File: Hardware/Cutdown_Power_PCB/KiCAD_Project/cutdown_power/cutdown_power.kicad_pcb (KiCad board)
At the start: 2 copper layers, 26.7 x 45.7 mm, 10 parts, among them J1 Control Signal, J2 Heater Coil, J3 Battery Pack, Q1 FQP30N06L

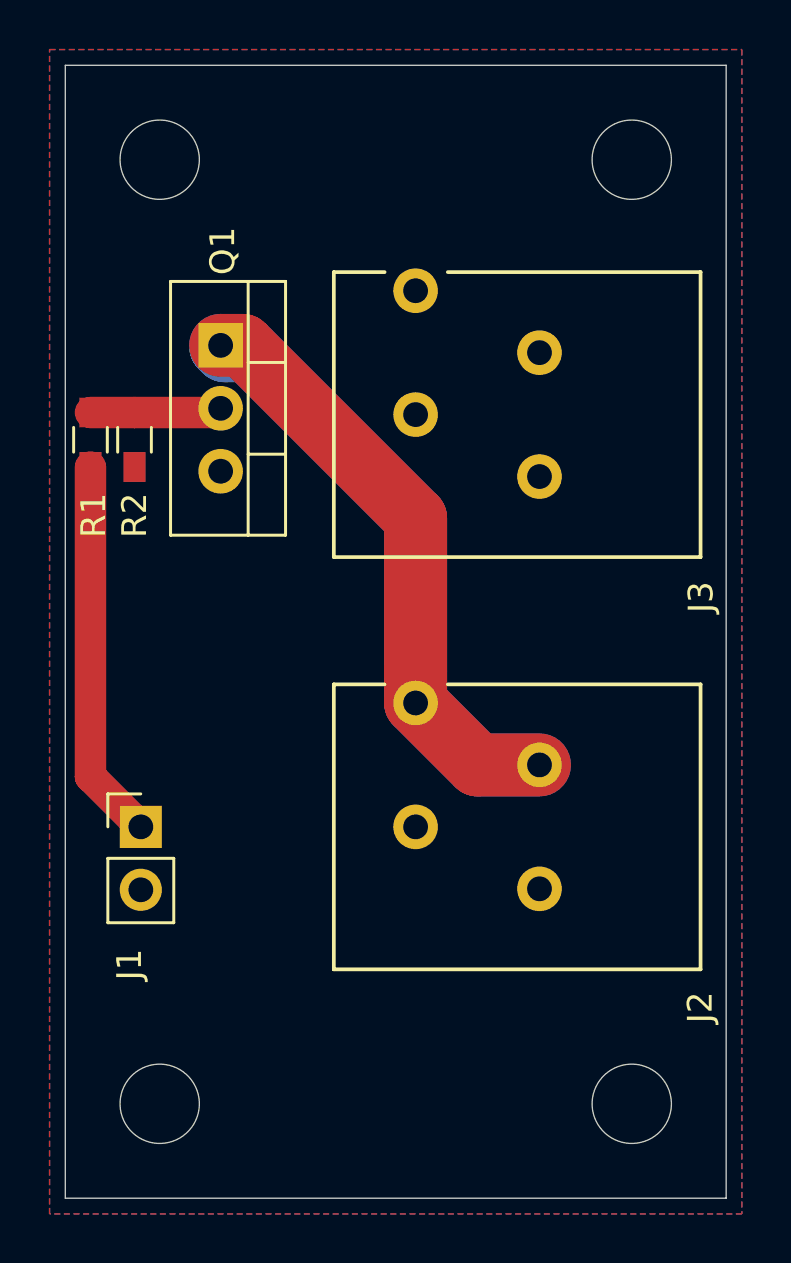
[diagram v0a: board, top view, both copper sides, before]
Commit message: Fix reversed Q1 issue and cut Rev 1.1
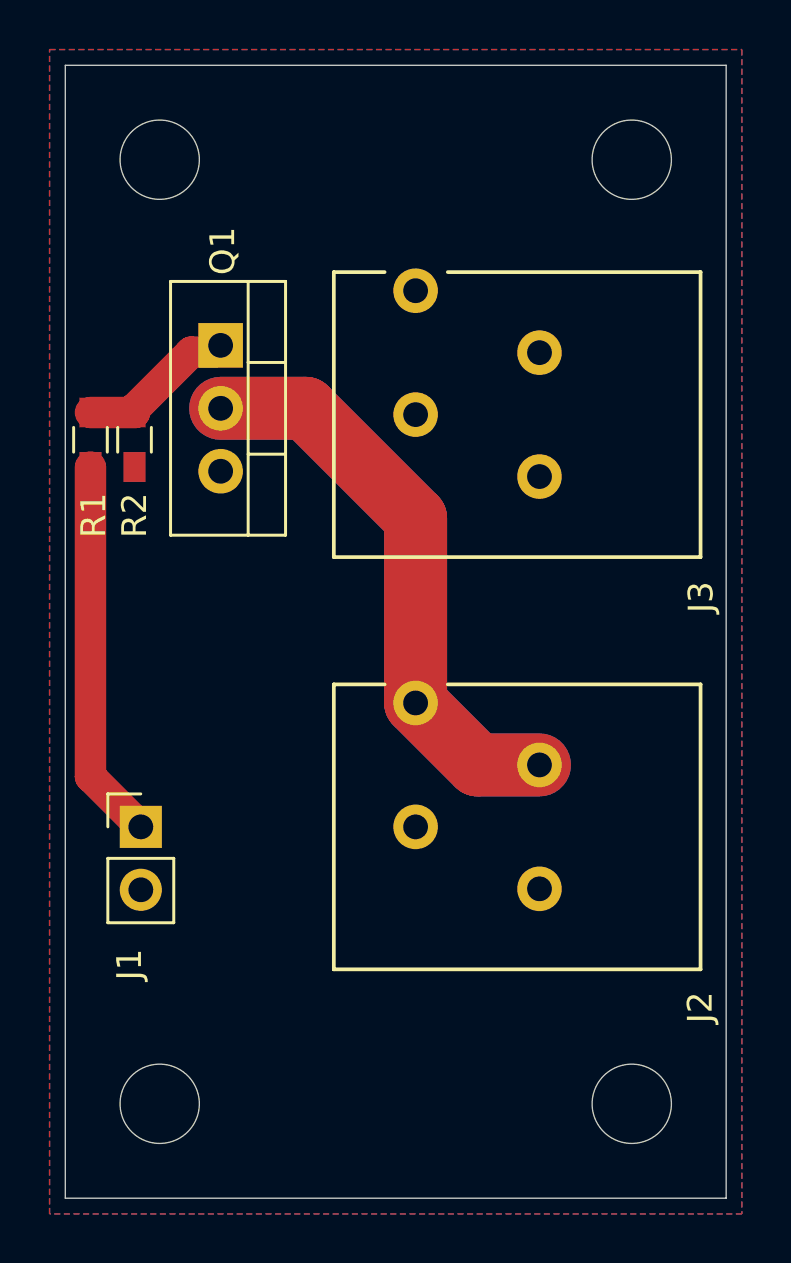
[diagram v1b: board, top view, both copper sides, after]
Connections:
- Q1 pad 1: Net-(J2-Pad2) -> Net-(Q1-Pad1)
- Q1 pad 2: Net-(Q1-Pad2) -> Net-(J2-Pad2)
- R1 pad 1: Net-(Q1-Pad2) -> Net-(Q1-Pad1)
- R2 pad 1: Net-(Q1-Pad2) -> Net-(Q1-Pad1)
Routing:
- net Net-(Q1-Pad1): track 0.00 -> 6.46 mm
- net Net-(Q1-Pad2): track 5.32 -> 0.00 mm
- net Net-(J2-Pad2): track 48.5 -> 46.4 mm
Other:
- board text added: "Leeman Geophysical LLC Cutdown Power Module Rev 1.1 December 2019 P/N 3-0000026"
- board text removed: "Leeman Geophysical LLC Cutdown Power Module Rev 1.0 November 2019 P/N 3-0000019"
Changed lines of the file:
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@@
     (thickness 1.6)
     (drawings 10)
-    (tracks 19)
+    (tracks 17)
     (zones 0)
     (modules 10)
@@
   (net 2 "Net-(J1-Pad1)")
   (net 3 "Net-(J2-Pad2)")
-  (net 4 "Net-(Q1-Pad2)")
-  (net 5 "Net-(J2-Pad1)")
+  (net 4 "Net-(J2-Pad1)")
+  (net 5 "Net-(Q1-Pad1)")
   (net_class Default "This is the default net class."
     (clearance 0.1524)
@@
     (add_net "Net-(J2-Pad1)")
     (add_net "Net-(J2-Pad2)")
-    (add_net "Net-(Q1-Pad2)")
+    (add_net "Net-(Q1-Pad1)")
   )
   (module Pin_Headers:Pin_Header_Straight_1x02_Pitch2.54mm (layer F.Cu)
@@
     (fp_line (start 5.75 -5.8) (end 5.75 -3.75) (layer F.SilkS) (width 0.15))
     (pad 1 thru_hole circle (at -2.5 2.5 90) (size 1.8 1.8) (drill 1) (layers *.Cu *.Mask)
-      (net 5 "Net-(J2-Pad1)"))
+      (net 4 "Net-(J2-Pad1)"))
     (pad 1 thru_hole circle (at 0 -2.5 90) (size 1.8 1.8) (drill 1) (layers *.Cu *.Mask)
-      (net 5 "Net-(J2-Pad1)"))
+      (net 4 "Net-(J2-Pad1)"))
     (pad 2 thru_hole circle (at 2.5 2.5 90) (size 1.8 1.8) (drill 1) (layers *.Cu *.Mask)
       (net 3 "Net-(J2-Pad2)"))
@@
       (net 1 GND))
     (pad 2 thru_hole oval (at 2.54 0 270) (size 1.8 1.8) (drill 1) (layers *.Cu *.Mask)
-      (net 4 "Net-(Q1-Pad2)"))
+      (net 3 "Net-(J2-Pad2)"))
     (pad 1 thru_hole rect (at 0 0 270) (size 1.8 1.8) (drill 1) (layers *.Cu *.Mask)
-      (net 3 "Net-(J2-Pad2)"))
+      (net 5 "Net-(Q1-Pad1)"))
     (model ${KISYS3DMOD}/TO_SOT_Packages_THT.3dshapes/TO-220-3_Vertical.wrl
       (offset (xyz 2.539999961853027 0 0))
@@
       (net 2 "Net-(J1-Pad1)"))
     (pad 1 smd rect (at -1.1 0 270) (size 1.2 0.9) (layers F.Cu F.Paste F.Mask)
-      (net 4 "Net-(Q1-Pad2)"))
+      (net 5 "Net-(Q1-Pad1)"))
     (model ${KISYS3DMOD}/Resistors_SMD.3dshapes/R_0603.wrl
       (at (xyz 0 0 0))
@@
     (fp_line (start 1.95 0.7) (end -1.96 0.7) (layer F.CrtYd) (width 0.05))
     (pad 1 smd rect (at -1.1 0 270) (size 1.2 0.9) (layers F.Cu F.Paste F.Mask)
-      (net 4 "Net-(Q1-Pad2)"))
+      (net 5 "Net-(Q1-Pad1)"))
     (pad 2 smd rect (at 1.1 0 270) (size 1.2 0.9) (layers F.Cu F.Paste F.Mask)
       (net 1 GND))
@@
       (net 1 GND))
     (pad 2 thru_hole circle (at 2.5 2.5 90) (size 1.8 1.8) (drill 1) (layers *.Cu *.Mask)
-      (net 5 "Net-(J2-Pad1)"))
+      (net 4 "Net-(J2-Pad1)"))
     (pad 2 thru_hole circle (at 5 -2.5 90) (size 1.8 1.8) (drill 1) (layers *.Cu *.Mask)
-      (net 5 "Net-(J2-Pad1)"))
+      (net 4 "Net-(J2-Pad1)"))
   )
   (module Mounting_Holes:MountingHole_3.2mm_M3_ISO7380 (layer F.Cu)
@@
   (gr_line (start 182.88 87.63) (end 182.88 133.35) (layer Edge.Cuts) (width 0.05))
   (gr_line (start 156.21 87.63) (end 182.88 87.63) (layer Edge.Cuts) (width 0.05))
-  (gr_text "Leeman Geophysical LLC\nCutdown Power Module\nRev 1.0 November 2019\nP/N 3-0000019\n" (at 169.545 91.44) (layer B.SilkS)
+  (gr_text "Leeman Geophysical LLC\nCutdown Power Module\nRev 1.1 December 2019\nP/N 3-0000026\n" (at 169.545 91.44) (layer B.SilkS)
     (effects (font (size 0.635 0.635) (thickness 0.15)) (justify mirror))
   )
@@
   (segment (start 157.226 116.332) (end 159.258 118.364) (width 1.27) (layer F.Cu) (net 2) (status 20))
   (segment (start 157.226 103.843) (end 157.226 116.332) (width 1.27) (layer F.Cu) (net 2) (status 10))
-  (segment (start 170.347 112.091208) (end 170.347 113.364) (width 2.54) (layer F.Cu) (net 3) (status 20))
-  (segment (start 170.347 105.903847) (end 170.347 112.091208) (width 2.54) (layer F.Cu) (net 3))
-  (segment (start 163.376153 98.933) (end 170.347 105.903847) (width 2.54) (layer F.Cu) (net 3) (status 10))
-  (segment (start 162.478999 98.933) (end 163.376153 98.933) (width 2.54) (layer F.Cu) (net 3) (status 30))
   (segment (start 172.847 115.864) (end 170.347 113.364) (width 2.54) (layer F.Cu) (net 3) (status 20))
   (segment (start 175.347 115.864) (end 172.847 115.864) (width 2.54) (layer F.Cu) (net 3) (status 10))
-  (segment (start 170.347 112.091208) (end 170.347 113.364) (width 2.54) (layer B.Cu) (net 3) (status 20))
-  (segment (start 170.347 105.903847) (end 170.347 112.091208) (width 2.54) (layer B.Cu) (net 3))
-  (segment (start 163.593752 99.150599) (end 170.347 105.903847) (width 2.54) (layer B.Cu) (net 3))
-  (segment (start 162.650599 99.150599) (end 163.593752 99.150599) (width 2.54) (layer B.Cu) (net 3) (status 10))
-  (segment (start 162.478999 98.933) (end 162.478999 98.978999) (width 2.54) (layer B.Cu) (net 3) (status 30))
-  (segment (start 162.478999 98.978999) (end 162.650599 99.150599) (width 2.54) (layer B.Cu) (net 3) (status 30))
   (segment (start 172.847 115.864) (end 170.347 113.364) (width 2.54) (layer B.Cu) (net 3) (status 20))
   (segment (start 175.347 115.864) (end 172.847 115.864) (width 2.54) (layer B.Cu) (net 3) (status 10))
-  (segment (start 157.226 101.643) (end 159.004 101.643) (width 1.27) (layer F.Cu) (net 4) (status 30))
-  (segment (start 162.308999 101.643) (end 162.478999 101.473) (width 1.27) (layer F.Cu) (net 4) (status 30))
-  (segment (start 159.004 101.643) (end 162.308999 101.643) (width 1.27) (layer F.Cu) (net 4) (status 30))
+  (segment (start 165.916153 101.473) (end 162.478999 101.473) (width 2.54) (layer F.Cu) (net 3))
+  (segment (start 170.347 113.364) (end 170.347 105.903847) (width 2.54) (layer F.Cu) (net 3))
+  (segment (start 170.347 105.903847) (end 165.916153 101.473) (width 2.54) (layer F.Cu) (net 3))
+  (segment (start 165.916153 101.473) (end 162.478999 101.473) (width 2.54) (layer B.Cu) (net 3))
+  (segment (start 170.347 113.364) (end 170.347 105.903847) (width 2.54) (layer B.Cu) (net 3))
+  (segment (start 170.347 105.903847) (end 165.916153 101.473) (width 2.54) (layer B.Cu) (net 3))
+  (segment (start 157.226 101.643) (end 159.004 101.643) (width 1.27) (layer F.Cu) (net 5))
+  (segment (start 159.004 101.493) (end 161.29 99.207) (width 1.27) (layer F.Cu) (net 5))
+  (segment (start 159.004 101.643) (end 159.004 101.493) (width 1.27) (layer F.Cu) (net 5))
+  (segment (start 162.204999 99.207) (end 162.478999 98.933) (width 1.27) (layer F.Cu) (net 5))
+  (segment (start 161.29 99.207) (end 162.204999 99.207) (width 1.27) (layer F.Cu) (net 5))
   (zone (net 1) (net_name GND) (layer F.Cu) (hatch edge 0.508)
     (connect_pads (clearance 0.508))
@@
     )
   )
-  (zone (net 5) (net_name "Net-(J2-Pad1)") (layer B.Cu) (hatch edge 0.508)
+  (zone (net 4) (net_name "Net-(J2-Pad1)") (layer B.Cu) (hatch edge 0.508)
     (connect_pads (clearance 0.508))
     (min_thickness 0.254)
